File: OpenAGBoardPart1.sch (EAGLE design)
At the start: 45 parts, among them U1 ARDUINO_SHIELDNO_SILK, U2 LM7805, U3 LD1117

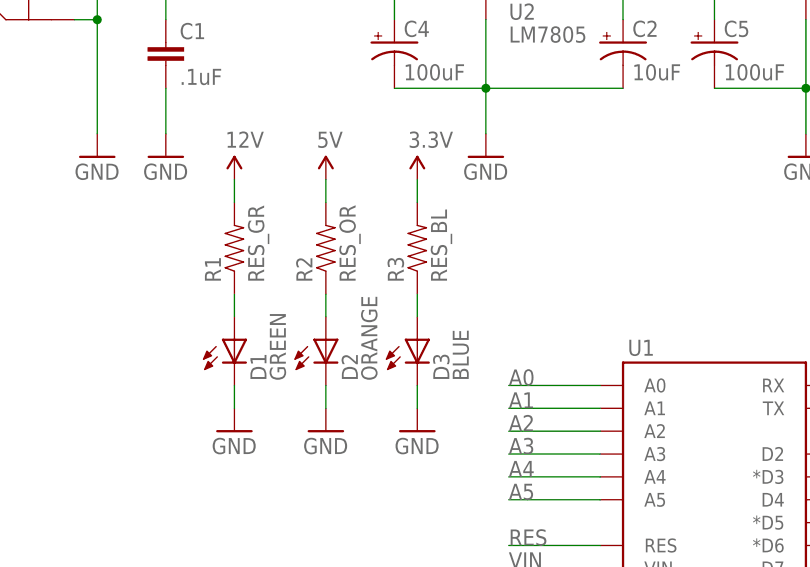
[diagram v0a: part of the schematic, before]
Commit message: Corrected LED color
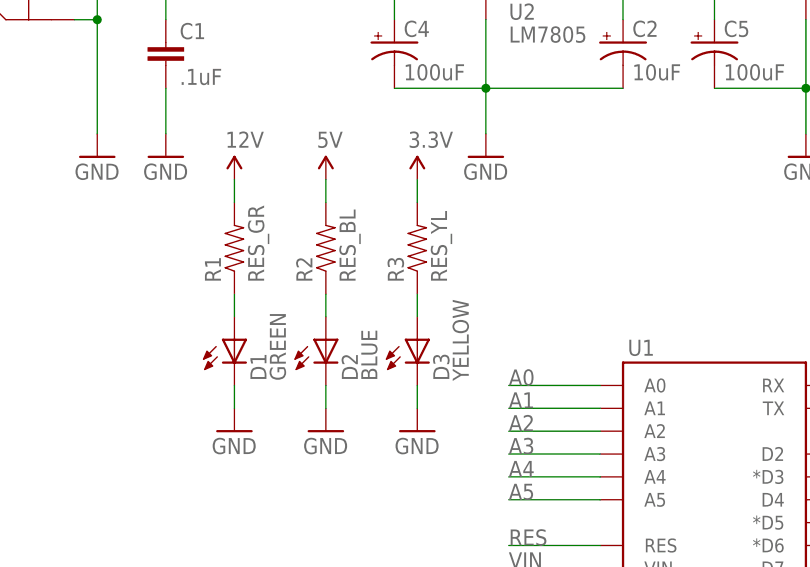
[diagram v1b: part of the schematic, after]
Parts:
- D2: value ORANGE -> BLUE
- D3: value BLUE -> YELLOW
- R2: value RES_OR -> RES_BL
- R3: value RES_BL -> RES_YL
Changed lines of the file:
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@@
 <part name="A_EXP" library="SparkFun-Connectors" deviceset="M02" device="PTH"/>
 <part name="U3" library="SparkFun-PowerIC" deviceset="V_REG_78XX" device="SINK" value="LD1117"/>
-<part name="D3" library="adafruit" deviceset="LED" device="5MM" value="BLUE"/>
-<part name="D2" library="adafruit" deviceset="LED" device="5MM" value="ORANGE"/>
+<part name="D3" library="adafruit" deviceset="LED" device="5MM" value="YELLOW"/>
+<part name="D2" library="adafruit" deviceset="LED" device="5MM" value="BLUE"/>
 <part name="D1" library="adafruit" deviceset="LED" device="5MM" value="GREEN"/>
 <part name="R1" library="SparkFun-Passives" deviceset="RESISTOR" device="PTH-1/4W" value="RES_GR"/>
-<part name="R2" library="SparkFun-Passives" deviceset="RESISTOR" device="PTH-1/4W" value="RES_OR"/>
-<part name="R3" library="SparkFun-Passives" deviceset="RESISTOR" device="PTH-1/4W" value="RES_BL"/>
+<part name="R2" library="SparkFun-Passives" deviceset="RESISTOR" device="PTH-1/4W" value="RES_BL"/>
+<part name="R3" library="SparkFun-Passives" deviceset="RESISTOR" device="PTH-1/4W" value="RES_YL"/>
 <part name="GND5" library="SparkFun-Aesthetics" deviceset="GND" device=""/>
 <part name="SUPPLY6" library="SparkFun-Aesthetics" deviceset="12V" device=""/>
